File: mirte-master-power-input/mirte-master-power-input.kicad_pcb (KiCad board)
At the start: 2 copper layers, 27.8 x 24.2 mm, 15 parts, among them J1 pwr_in, J2 battery, J3 robot, Q1 DMMT5401, Q2 SiA483DJ, Q3 DMMT5401, Q4 SiA483DJ

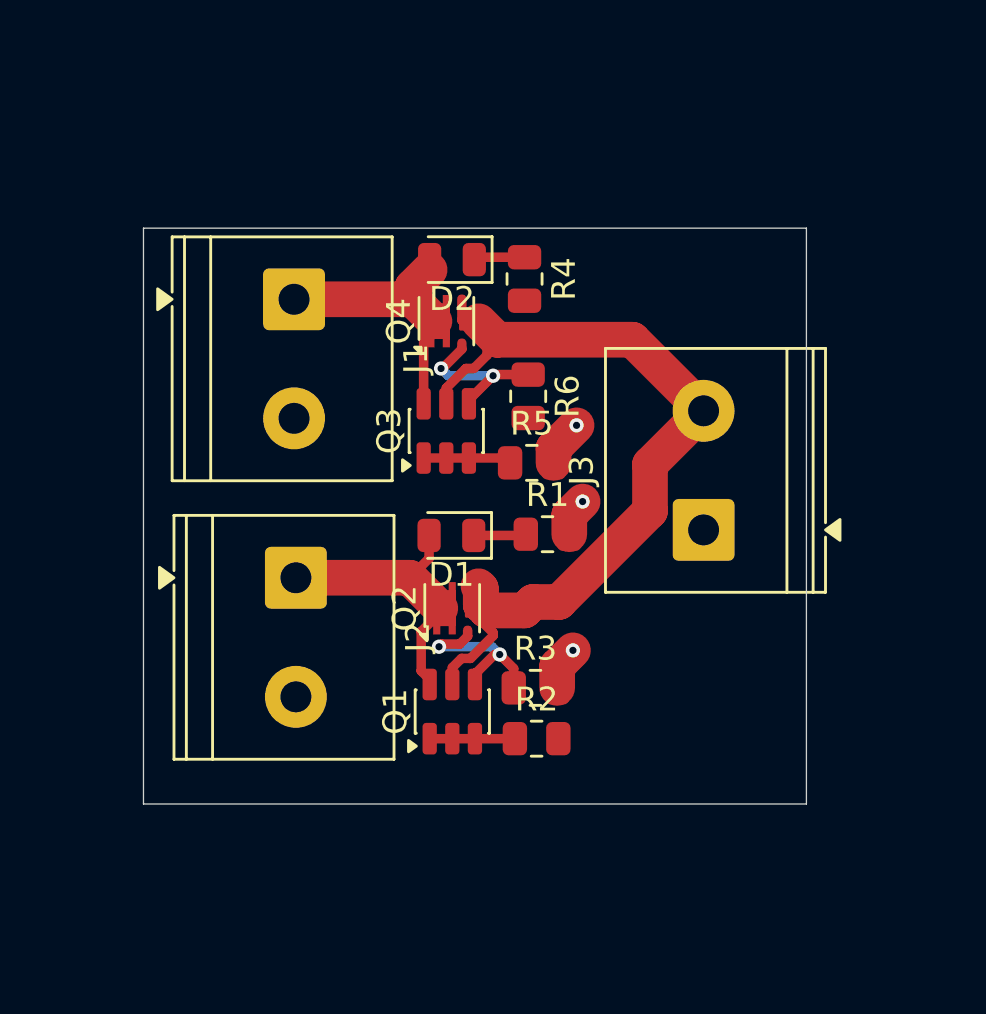
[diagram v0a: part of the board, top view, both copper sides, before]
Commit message: Power input: fix layout & fix diode setup
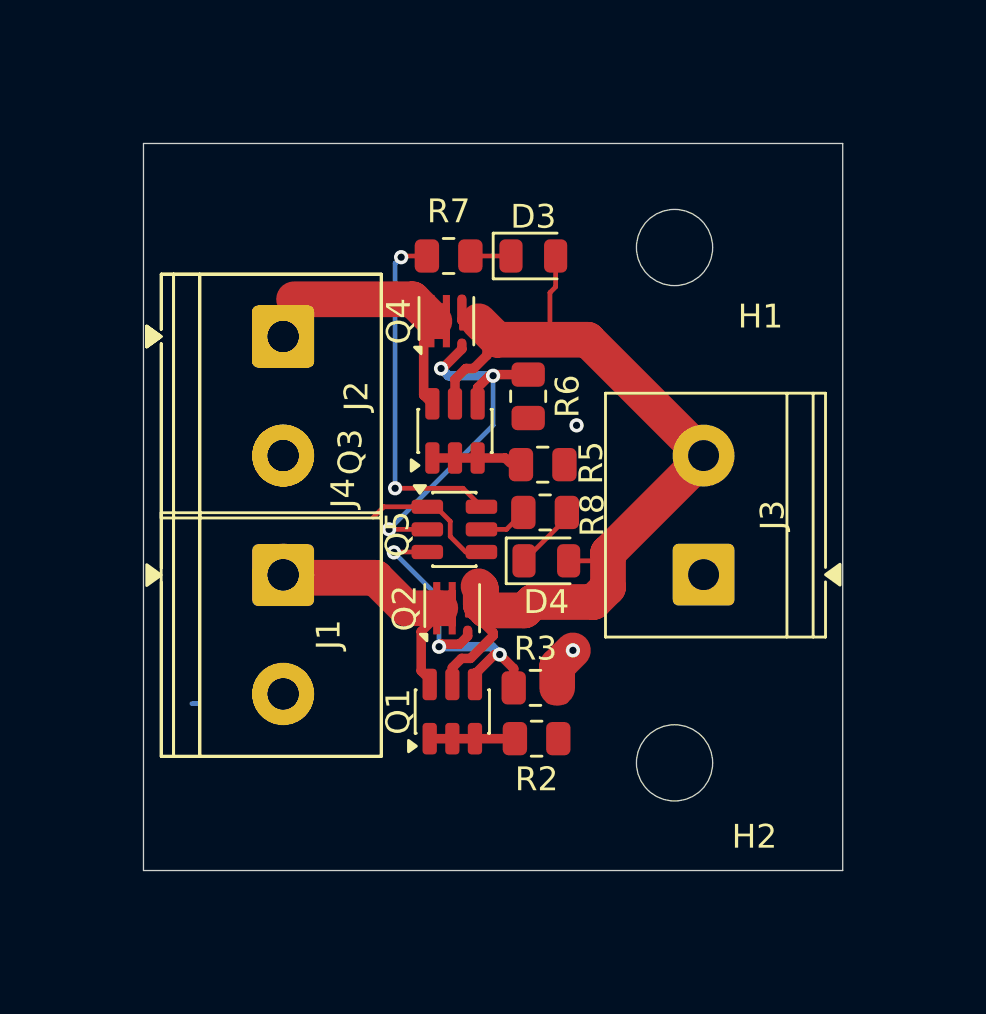
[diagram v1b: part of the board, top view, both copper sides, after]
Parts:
- removed D1, D2: LED, LED_SMD:LED_0805_2012Metric
- removed R1, R4: 10k, Resistor_SMD:R_0805_2012Metric
- added D3: LED, LED_SMD:LED_0805_2012Metric, F.Cu at (108.6, 61.0)
- added D4: LED, LED_SMD:LED_0805_2012Metric, F.Cu at (109.1, 73.8)
- added H1: MountingHole, MountingHole:MountingHole_3.2mm_M3, F.Cu at (114.5, 60.6)
- added H2: MountingHole, MountingHole:MountingHole_3.2mm_M3, F.Cu at (114.5, 82.2)
- added J4: Screw_Terminal_01x04, TerminalBlock_Phoenix:TerminalBlock_Phoenix_PT-1,5-4-5.0-H_1x04_P5.00mm_Horizontal, F.Cu at (98.1, 64.3)
- added Q5: DMMT5401, Package_TO_SOT_SMD:SOT-23-6, F.Cu at (105.3, 72.4)
- added R7: 10k, Resistor_SMD:R_0805_2012Metric, F.Cu at (105.0, 61.0)
- added R8: 10k, Resistor_SMD:R_0805_2012Metric, F.Cu at (109.1, 71.7)
- moved J1 11.6 mm to (98.1, 74.4)
- moved J2 10.1 mm to (98.1, 64.3)
- moved J3 1.88 mm to (115.7, 74.3)
- moved R5 0.46 mm to (109.0, 69.7)
- moved Q3 0.37 mm to (105.3, 68.3)
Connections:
- net /ideal_diode/V_out renamed /Vout
- net Net-(Q1B-C2) renamed /mos_sig2
- net Net-(Q3B-C2) renamed /mos_sig1
- J1 pad 1: /ideal_diode1/V_in -> /ideal_diode/V_in
- J2 pad 1: /ideal_diode/V_in -> /ideal_diode1/V_in
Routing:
- net Net-(Q5A-E1): track 0.00 -> 14.9 mm, vias 0 -> 2
- net /mos_sig1: track 6.86 -> 16.7 mm, vias 2 -> 3
- net /mos_sig2: track 7.58 -> 13.7 mm, vias 2 -> 3
- net /Vout: track 36.0 -> 40.3 mm
- net Net-(D4-K): track 0.00 -> 2.78 mm
- net GND: track 5.43 -> 7.74 mm, vias 3 -> 2
- net Net-(D1-K): track 2.21 -> 0.00 mm
- net Net-(D2-K): track 2.15 -> 0.00 mm
- net /ideal_diode/V_in: track 12.2 -> 10.1 mm
- net Net-(Q5B-E2): track 0.00 -> 2.05 mm
- net Net-(D3-K): track 0.00 -> 1.71 mm
- net /ideal_diode1/V_in: track 11.5 -> 10.2 mm
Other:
- board size 27.8 x 24.2 mm -> 29.4 x 30.5 mm
- board text added: "12V in GND 12V in GND"
- board text added: "12V out GND"
